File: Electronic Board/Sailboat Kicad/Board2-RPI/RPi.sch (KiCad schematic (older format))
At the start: 1 part, among them J23 Conn_02x20_Odd_Even

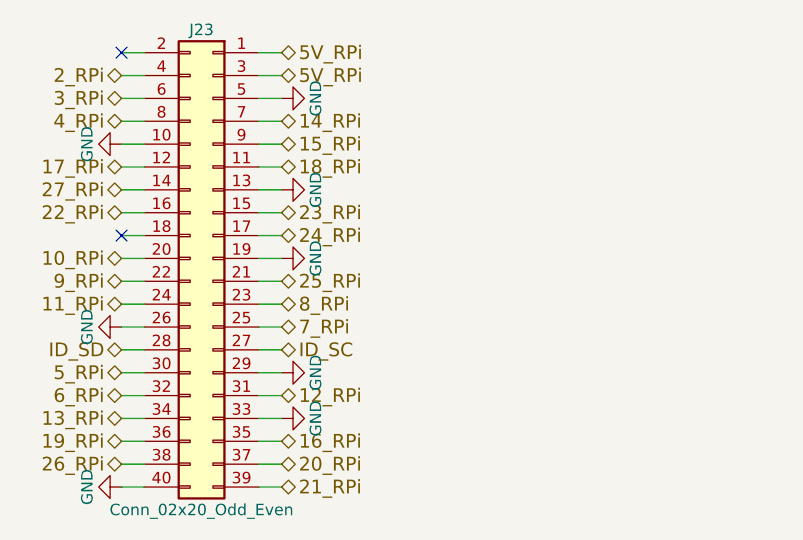
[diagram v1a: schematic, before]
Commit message: Cleaned up, and added security, text and better usability, preparation for board v2
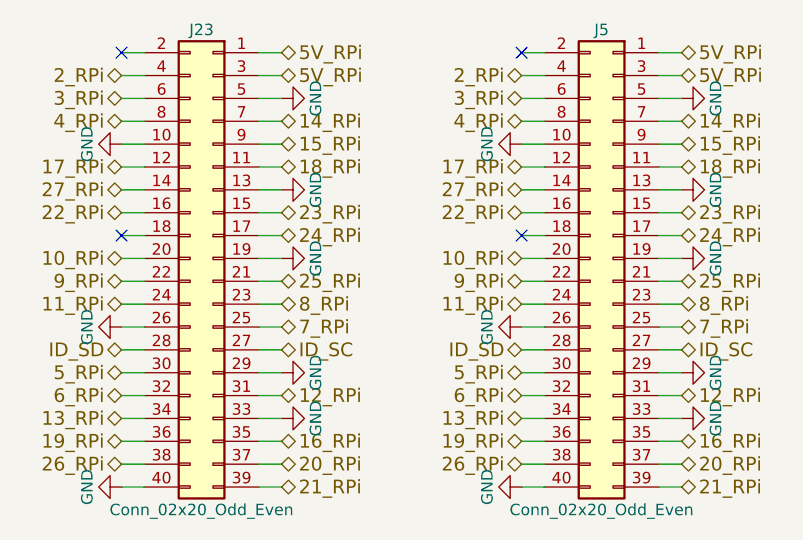
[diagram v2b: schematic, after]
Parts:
- added J5: Conn_02x20_Odd_Even, Pin_Headers:Pin_Header_Straight_2x20_Pitch2.54mm, symbol Conn_02x20_Odd_Even
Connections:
- net 10_RPi: now also J5.20 (Pin_20)
- net 11_RPi: now also J5.24 (Pin_24)
- net 12_RPi: now also J5.31 (Pin_31)
- net 13_RPi: now also J5.34 (Pin_34)
- net 14_RPi: now also J5.7 (Pin_7)
- net 15_RPi: now also J5.9 (Pin_9)
- net 16_RPi: now also J5.35 (Pin_35)
- net 17_RPi: now also J5.12 (Pin_12)
- net 18_RPi: now also J5.11 (Pin_11)
- net 19_RPi: now also J5.36 (Pin_36)
- net 20_RPi: now also J5.37 (Pin_37)
- net 21_RPi: now also J5.39 (Pin_39)
- net 22_RPi: now also J5.16 (Pin_16)
- net 23_RPi: now also J5.15 (Pin_15)
- net 24_RPi: now also J5.17 (Pin_17)
- net 25_RPi: now also J5.21 (Pin_21)
- net 26_RPi: now also J5.38 (Pin_38)
- net 27_RPi: now also J5.14 (Pin_14)
- net 2_RPi: now also J5.4 (Pin_4)
- net 3_RPi: now also J5.6 (Pin_6)
- net 4_RPi: now also J5.8 (Pin_8)
- net 5V_RPi: now also J5.1 (Pin_1), J5.3 (Pin_3)
- net 5_RPi: now also J5.30 (Pin_30)
- net 6_RPi: now also J5.32 (Pin_32)
- net 7_RPi: now also J5.25 (Pin_25)
- net 8_RPi: now also J5.23 (Pin_23)
- net 9_RPi: now also J5.22 (Pin_22)
- net GND: now also J5.10 (Pin_10), J5.13 (Pin_13), J5.19 (Pin_19), J5.26 (Pin_26), J5.29 (Pin_29), J5.33 (Pin_33), J5.40 (Pin_40), J5.5 (Pin_5)
- net ID_SC: now also J5.27 (Pin_27)
- net ID_SD: now also J5.28 (Pin_28)
- no-connect marks 2 -> 4
